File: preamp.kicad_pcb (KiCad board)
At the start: 2 copper layers, 29.5 x 25.4 mm, 19 parts, among them P1 RCA_IN, P2 Power, P3 RCA_OUT, U1 TL071

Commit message: First rev complete.
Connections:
- R1 pad 2: Net-(R1-Pad2) -> GND
- R2 pad 2: Net-(R1-Pad2) -> GND
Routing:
- net GND: track 0.00 -> 4.69 mm, vias 0 -> 2
- net Net-(C2-Pad2): track 5.93 -> 6.57 mm
- added copper zone on B.Cu, net GND
- added copper zone on F.Cu, net GND
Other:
- board size 29.5 x 25.4 mm -> 30.5 x 25.4 mm

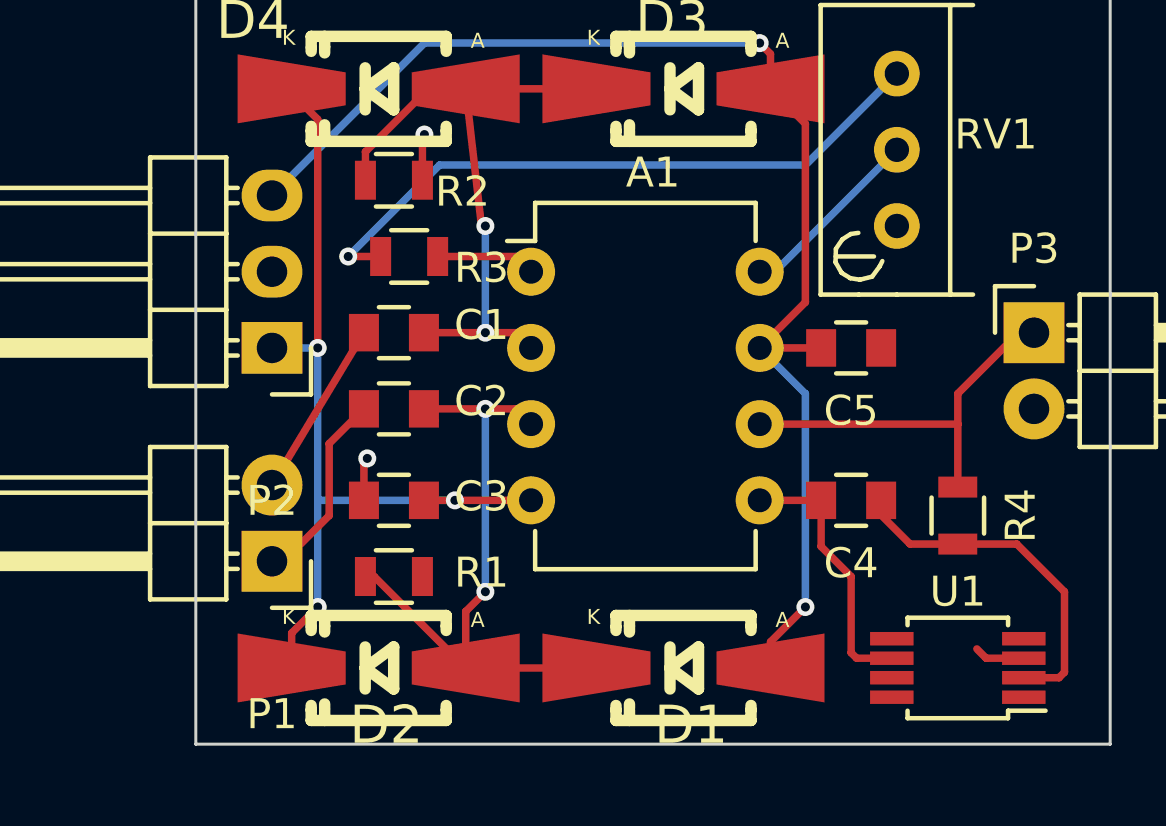
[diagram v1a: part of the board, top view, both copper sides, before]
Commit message: Add silkscreen labels for IO
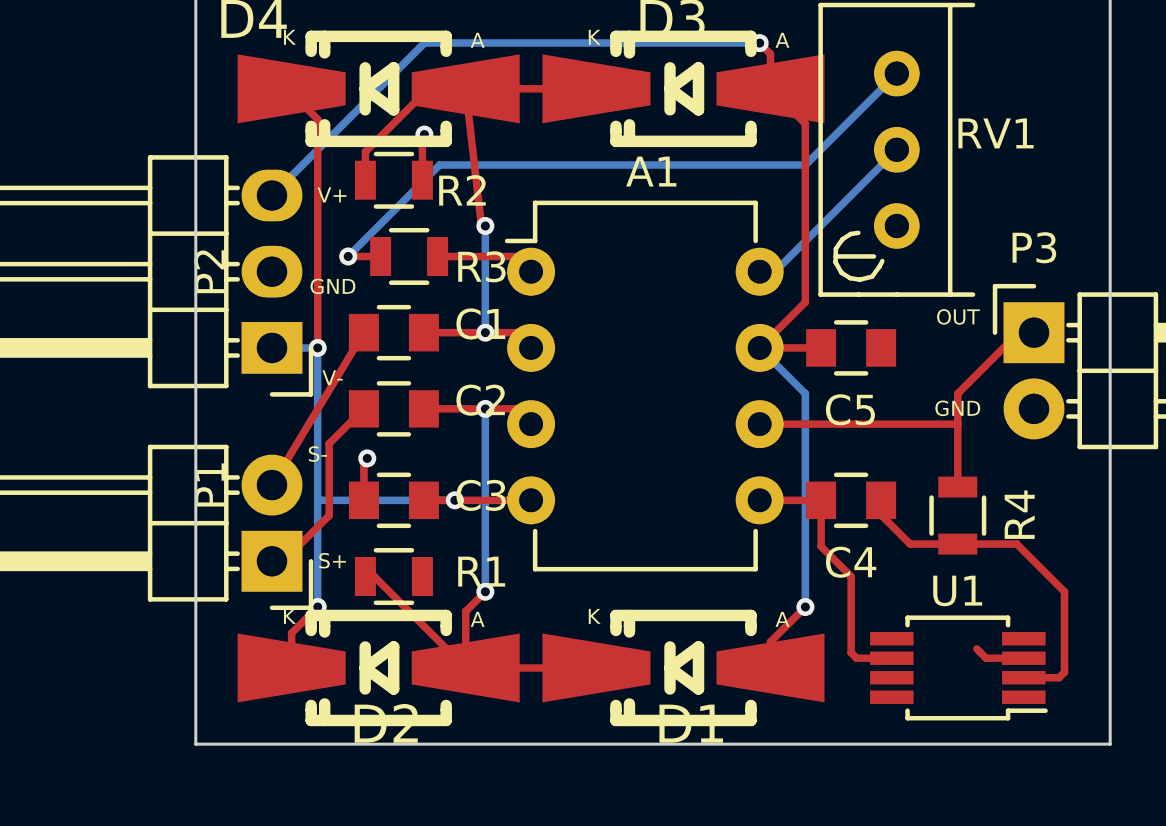
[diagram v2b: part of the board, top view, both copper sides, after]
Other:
- board text added: "GND"
- board text added: "OUT"
- board text added: "S+"
- board text added: "S-"
- board text added: "V+"
- board text added: "V-"

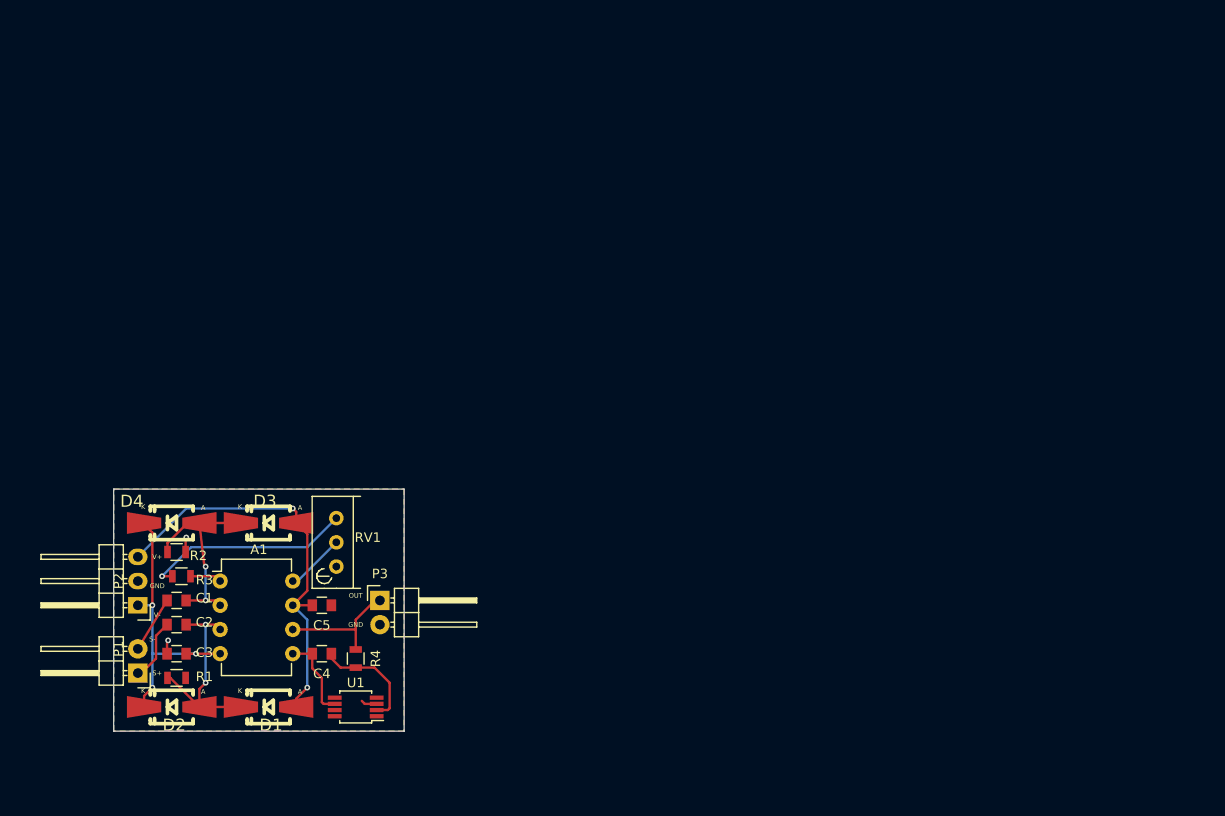
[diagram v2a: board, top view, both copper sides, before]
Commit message: Expand to stereo, add AC power supply.  Not done yet.
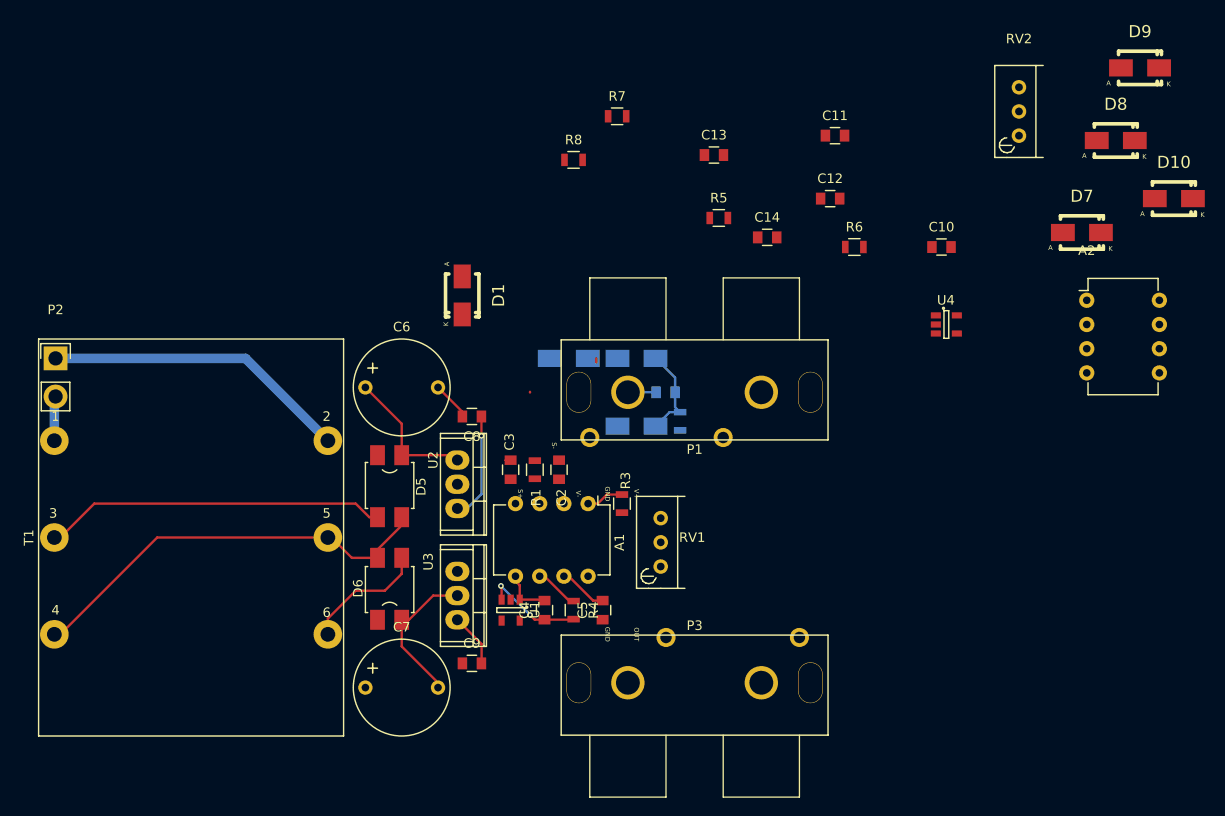
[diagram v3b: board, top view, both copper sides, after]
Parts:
- added A2: INA217, Housings_DIP:DIP-8_W7.62mm, F.Cu at (150.4, 53.8)
- added C10: 1uf, Capacitors_SMD:C_0805, F.Cu at (135.1, 48.3)
- added C11: 1uf, Capacitors_SMD:C_0805, F.Cu at (124.0, 36.6)
- added C12: 0.1uf, Capacitors_SMD:C_0805, F.Cu at (123.4, 43.2)
- added C13: 0.1uf, Capacitors_SMD:C_0805, F.Cu at (111.3, 38.6)
- added C14: 0.1uf, Capacitors_SMD:C_0805, F.Cu at (116.8, 47.2)
- added C6: 1000uF, Capacitors_Elko_ThroughHole:Elko_vert_20x10mm_RM7.5, F.Cu at (74.7, 63.0)
- added C7: 1000uF, Capacitors_Elko_ThroughHole:Elko_vert_20x10mm_RM7.5, F.Cu at (74.7, 94.5)
- added C8: 0.1uF, Capacitors_SMD:C_0805, F.Cu at (85.9, 66.0)
- added C9: 1uF t, Capacitors_SMD:C_0805, F.Cu at (85.9, 91.9)
- added D10: D, Dioden_SMD_RevA_06Sep2012:Diode-SMA_Standard_RevA_26July2010, F.Cu at (159.5, 43.2)
- added D5: Diode_Bridge, preamp:Bridge-Rectifier-SOIC-4, F.Cu at (77.2, 73.2)
- added D6: Diode_Bridge, preamp:Bridge-Rectifier-SOIC-4, F.Cu at (77.2, 84.3)
- added D7: D, Dioden_SMD_RevA_06Sep2012:Diode-SMA_Standard_RevA_26July2010, F.Cu at (149.9, 46.7)
- added D8: D, Dioden_SMD_RevA_06Sep2012:Diode-SMA_Standard_RevA_26July2010, F.Cu at (153.4, 37.1)
- added D9: D, Dioden_SMD_RevA_06Sep2012:Diode-SMA_Standard_RevA_26July2010, F.Cu at (156.0, 29.5)
- added R5: 2.2k, Resistors_SMD:R_0805, F.Cu at (111.8, 45.2)
- added R6: 2.2k, Resistors_SMD:R_0805, F.Cu at (126.0, 48.3)
- added R7: 1k, Resistors_SMD:R_0805, F.Cu at (101.1, 34.5)
- added R8: 1M, Resistors_SMD:R_0805, F.Cu at (96.5, 39.1)
- added RV2: 10k, Potentiometers:Potentiometer_Bourns_3296W_3-8Zoll_Inline_ScrewUp, F.Cu at (143.3, 36.6)
- added T1: TRANSFO2, preamp:preamp_transformer_6pin, F.Cu at (56.4, 78.7)
- added U2: LM7815CT, Power_Integrations:TO-220, F.Cu at (84.3, 73.2)
- added U3: LM7915CT, Power_Integrations:TO-220, F.Cu at (84.3, 84.8)
- added U4: OPA137N, Housings_SOT-23_SOT-143_TSOT-6:SOT-23-5, F.Cu at (135.6, 56.4)
- C1, R2: moved to B.Cu
- D1: footprint Dioden_SMD_RevA_06Sep2012:Diode-Universal-SMA-SMB_Handsoldering_RevA_27July2010 -> Dioden_SMD_RevA_06Sep2012:Diode-SMA_Standard_RevA_26July2010
- D2, D3, D4: footprint Dioden_SMD_RevA_06Sep2012:Diode-Universal-SMA-SMB_Handsoldering_RevA_27July2010 -> Dioden_SMD_RevA_06Sep2012:Diode-SMA_Standard_RevA_26July2010; moved to B.Cu
- P1: value RCA_IN -> CONN_01X04; footprint Pin_Headers:Pin_Header_Angled_1x02 -> preamp:preamp_RCA_STEREO
- P2: value Power -> CONN_01X02; footprint Pin_Headers:Pin_Header_Angled_1x03 -> preamp:Power_Pin_Header
- P3: value RCA_OUT -> CONN_01X04; footprint Pin_Headers:Pin_Header_Angled_1x02 -> preamp:preamp_RCA_STEREO
- U1: value TL071 -> OPA137N; footprint Housings_SSOP:MSOP-8_3x3mm_Pitch0.65mm -> Housings_SOT-23_SOT-143_TSOT-6:SOT-23-5
- moved P1 65.4 mm to (109.2, 63.5), turned to 0 degrees
- moved C1 55.8 mm to (106.2, 63.5)
- moved D2 55.4 mm to (96.0, 59.9), turned to 0 degrees
- moved R2 54.6 mm to (107.7, 66.5), turned to 270 degrees
- moved D4 51.7 mm to (103.1, 59.9)
- moved D1 47.7 mm to (84.8, 53.3), turned to 270 degrees
- moved R3 46.9 mm to (101.6, 75.2), turned to 90 degrees
- moved R1 43.5 mm to (92.5, 71.6), turned to 270 degrees
- moved C2 43.3 mm to (95.0, 71.6), turned to 90 degrees
- moved C3 40.0 mm to (89.9, 71.6), turned to 90 degrees
- moved D3 39.9 mm to (103.1, 67.1), turned to 0 degrees
- moved A1 39.5 mm to (98.0, 75.2), turned to 270 degrees
- moved P3 34.1 mm to (109.2, 94.0), turned to 180 degrees
- moved RV1 34.0 mm to (105.7, 81.8)
- moved C5 29.5 mm to (99.6, 86.4), turned to 90 degrees
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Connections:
- P1 pad 1: Net-(C2-Pad2) -> Net-(C10-Pad2)
- P1 pad 2: Net-(C1-Pad2) -> Net-(C11-Pad2)
- P2 pad 1: -15V -> Earth
- P2 pad 2: GND -> VCC
- P3 pad 1: Net-(A1-Pad6) -> GND
- P3 pad 2: GND -> Net-(A2-Pad6)
- U1 pad 1: (no net) -> Net-(A1-Pad5)
- U1 pad 2: Net-(C4-Pad1) -> Net-(U1-Pad2)
- U1 pad 3: GND -> Net-(C4-Pad1)
- U1 pad 4: Net-(U1-Pad4) -> GND
- U1 pad 5: (no net) -> Net-(U1-Pad5)
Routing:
- net Net-(D5-Pad2): track 0.00 -> 44.3 mm
- net Net-(D5-Pad4): track 0.00 -> 36.0 mm
- net Earth: track 0.00 -> 32.7 mm
- net +15V: track 43.6 -> 17.1 mm, vias 2 -> 1
- net -15V: track 30.6 -> 6.68 mm, vias 3 -> 0
- net Net-(A1-Pad3): track 22.6 -> 0.08 mm, vias 2 -> 0
- net Net-(R3-Pad1): track 21.9 -> 0.00 mm, vias 1 -> 0
- net Net-(C7-Pad2): track 0.00 -> 15.6 mm
- net Net-(C6-Pad1): track 0.00 -> 14.7 mm
- net Net-(D6-Pad4): track 0.00 -> 13.0 mm
- net Net-(A1-Pad2): track 22.5 -> 10.4 mm, vias 2 -> 0
- net Net-(A1-Pad6): track 13.1 -> 4.64 mm
- net Net-(C2-Pad2): track 6.57 -> 0.00 mm
- net Net-(A1-Pad8): track 6.26 -> 0.00 mm
- net VCC: track 0.00 -> 4.69 mm
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- removed copper zone on B.Cu, net GND
- removed copper zone on F.Cu, net GND
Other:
- board outline removed
- net class AC_PWR added: clearance 0.2, trace_width 1, via_dia 0.6, via_drill 0.4

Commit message: More work on stereo plus PCB footprint
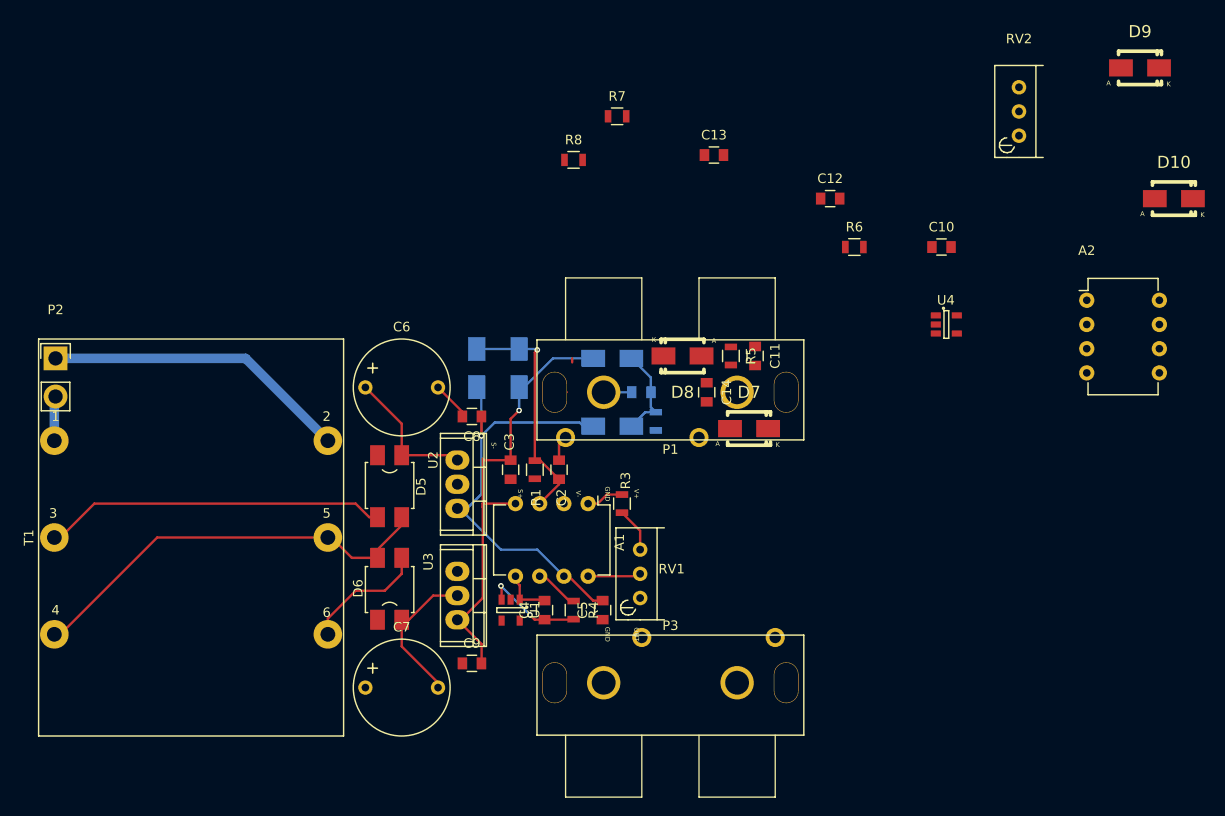
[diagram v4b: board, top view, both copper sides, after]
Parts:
- D1: moved to B.Cu
- moved D8 50.8 mm to (108.0, 59.7), turned to 180 degrees
- moved D7 40.5 mm to (114.9, 67.3)
- moved C11 24.6 mm to (115.6, 59.7), turned to 270 degrees
- moved C14 17.5 mm to (110.5, 63.5), turned to 270 degrees
- moved R5 14.5 mm to (113.0, 59.7), turned to 270 degrees
- moved D1 7.77 mm to (86.4, 61.0), turned to 90 degrees
- moved D2 5.31 mm to (90.8, 61.0), turned to 270 degrees
- moved RV1 3.95 mm to (103.5, 85.1)
- moved C1 2.54 mm to (103.6, 63.5)
- moved D3 2.54 mm to (100.6, 67.1)
- moved D4 2.54 mm to (100.6, 59.9)
- moved P1 2.54 mm to (106.7, 63.5)
- moved P3 2.54 mm to (106.7, 94.0)
- moved R2 2.54 mm to (105.2, 66.5)
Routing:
- net -15V: track 6.68 -> 48.8 mm, vias 0 -> 1
- net +15V: track 17.1 -> 49.0 mm
- net Net-(A1-Pad3): track 0.08 -> 24.9 mm, vias 0 -> 1
- net Net-(A1-Pad8): track 0.00 -> 5.57 mm
- net Net-(R3-Pad1): track 0.00 -> 4.67 mm
- net Net-(C2-Pad2): track 0.00 -> 2.66 mm
- net Net-(C1-Pad2): track 2.95 -> 1.68 mm

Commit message: More footprint improvements.
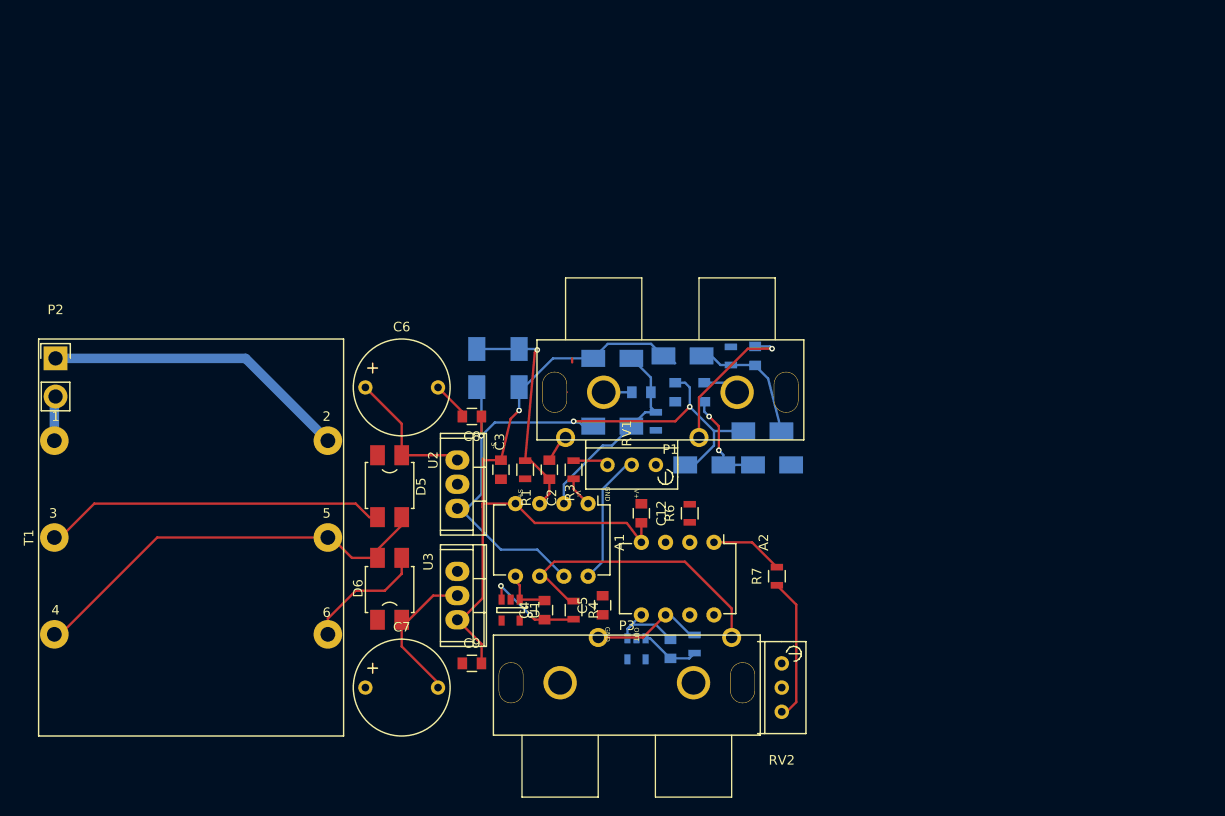
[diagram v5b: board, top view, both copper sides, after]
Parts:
- C10, C11, C13, C14, D10, D7, D8, D9, R5, R8, U4: moved to B.Cu
- moved D9 61.9 mm to (110.2, 71.1)
- moved RV2 60.7 mm to (118.4, 91.9), turned to 180 degrees
- moved R8 52.4 mm to (109.2, 89.9), turned to 270 degrees
- moved C13 52.0 mm to (106.7, 90.4), turned to 90 degrees
- moved R7 51.1 mm to (117.9, 82.8), turned to 90 degrees
- moved D10 50.6 mm to (117.3, 71.1)
- moved U4 47.1 mm to (103.1, 90.4), turned to 270 degrees
- moved A2 46.6 mm to (111.3, 79.2), turned to 270 degrees
- moved C12 38.5 mm to (103.6, 76.2), turned to 270 degrees
- moved R6 32.8 mm to (108.7, 76.2), turned to 90 degrees
- moved C10 29.2 mm to (110.2, 63.5), turned to 90 degrees
- moved RV1 14.1 mm to (105.2, 71.1), turned to 90 degrees
- moved R3 6.20 mm to (96.5, 71.6), turned to 270 degrees
- moved P3 4.57 mm to (102.1, 94.0)
- moved C14 3.30 mm to (107.2, 63.5), turned to 90 degrees
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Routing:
- net -15V: track 48.8 -> 75.0 mm
- net Net-(A1-Pad6): track 4.64 -> 30.5 mm
- net +15V: track 49.0 -> 73.3 mm, vias 1 -> 3
- net Net-(C11-Pad2): track 0.00 -> 15.9 mm, vias 0 -> 1
- net Net-(R7-Pad1): track 0.00 -> 15.0 mm
- net Net-(A2-Pad3): track 0.00 -> 13.6 mm
- net Net-(A2-Pad6): track 0.00 -> 12.0 mm
- net Net-(A1-Pad2): track 10.4 -> 22.1 mm
- net Net-(A2-Pad2): track 0.00 -> 10.6 mm, vias 0 -> 2
- net Net-(A2-Pad5): track 0.00 -> 8.40 mm
- net Net-(A1-Pad8): track 5.57 -> 13.9 mm
- net Net-(A2-Pad1): track 0.00 -> 7.68 mm
- net Net-(C13-Pad1): track 0.00 -> 6.25 mm
- net Net-(C10-Pad2): track 0.00 -> 3.86 mm
- net Net-(A1-Pad1): track 6.34 -> 3.68 mm
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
